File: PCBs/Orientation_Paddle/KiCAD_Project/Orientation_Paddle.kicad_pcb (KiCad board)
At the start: 2 copper layers, 108 x 47 mm, 76 parts, among them J1 NP_Conn_01x04_Relief, J10 1-0000190, J2 1-0001205, J3 NP_Conn_01x03_Relief, J4 NP_Conn_01x02_Relief, J5 NP_Conn_01x02_Relief, J6 NP_Conn_01x04, J7 NP_Conn_01x04, J8 NP_Conn_01x02, J9 1-0000050, U1 1-0001232, U2 1-0001471, U3 1-0000207, U4 1-0000446, U5 1-0000785, Y1 1-0000721

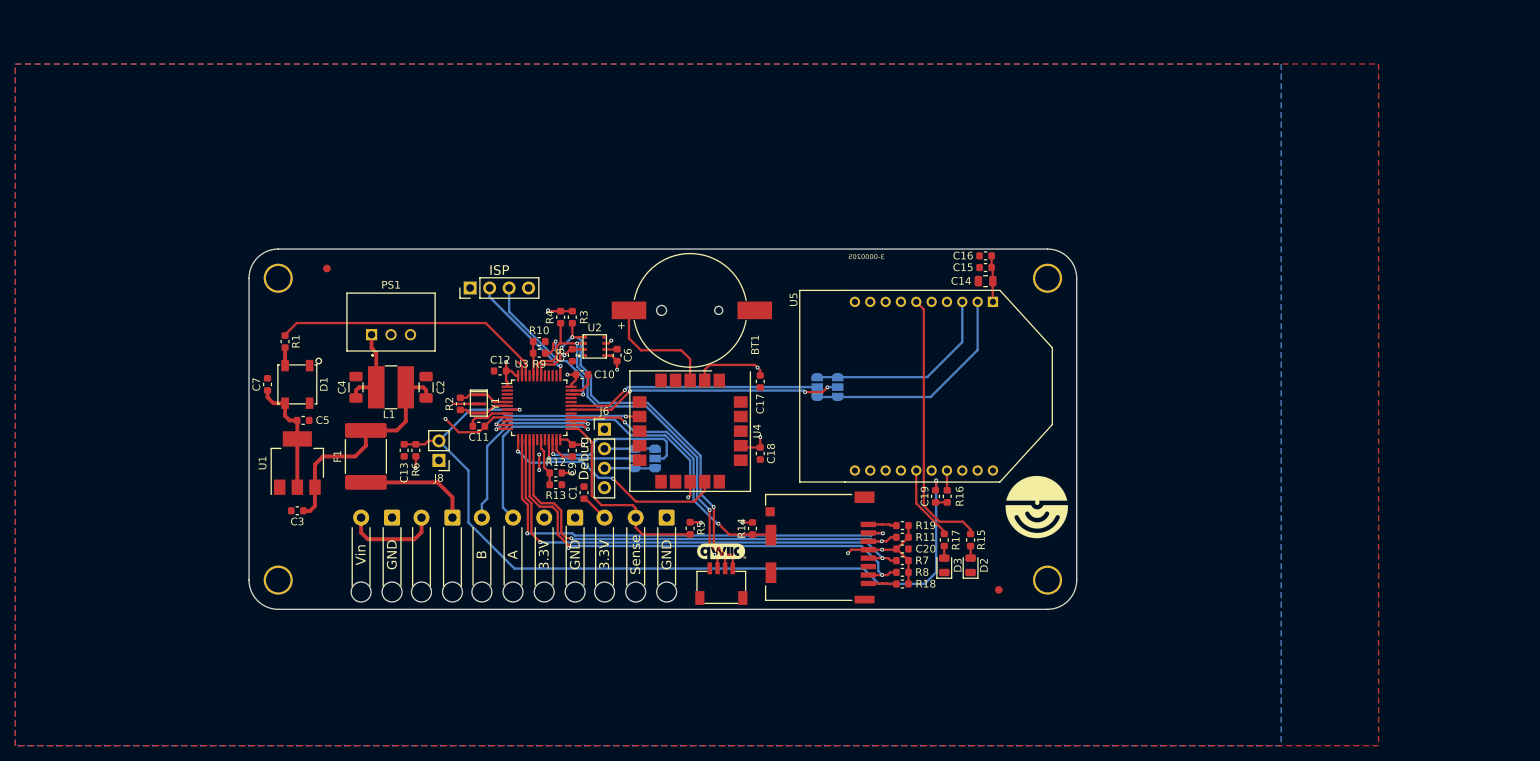
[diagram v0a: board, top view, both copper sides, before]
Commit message: Orientation Paddle Revisions: Board resize to nice numbers Fixed Footprint/Symbols causing ERC Errors Fixed remaining ERC Errors (Schematic and PCB)
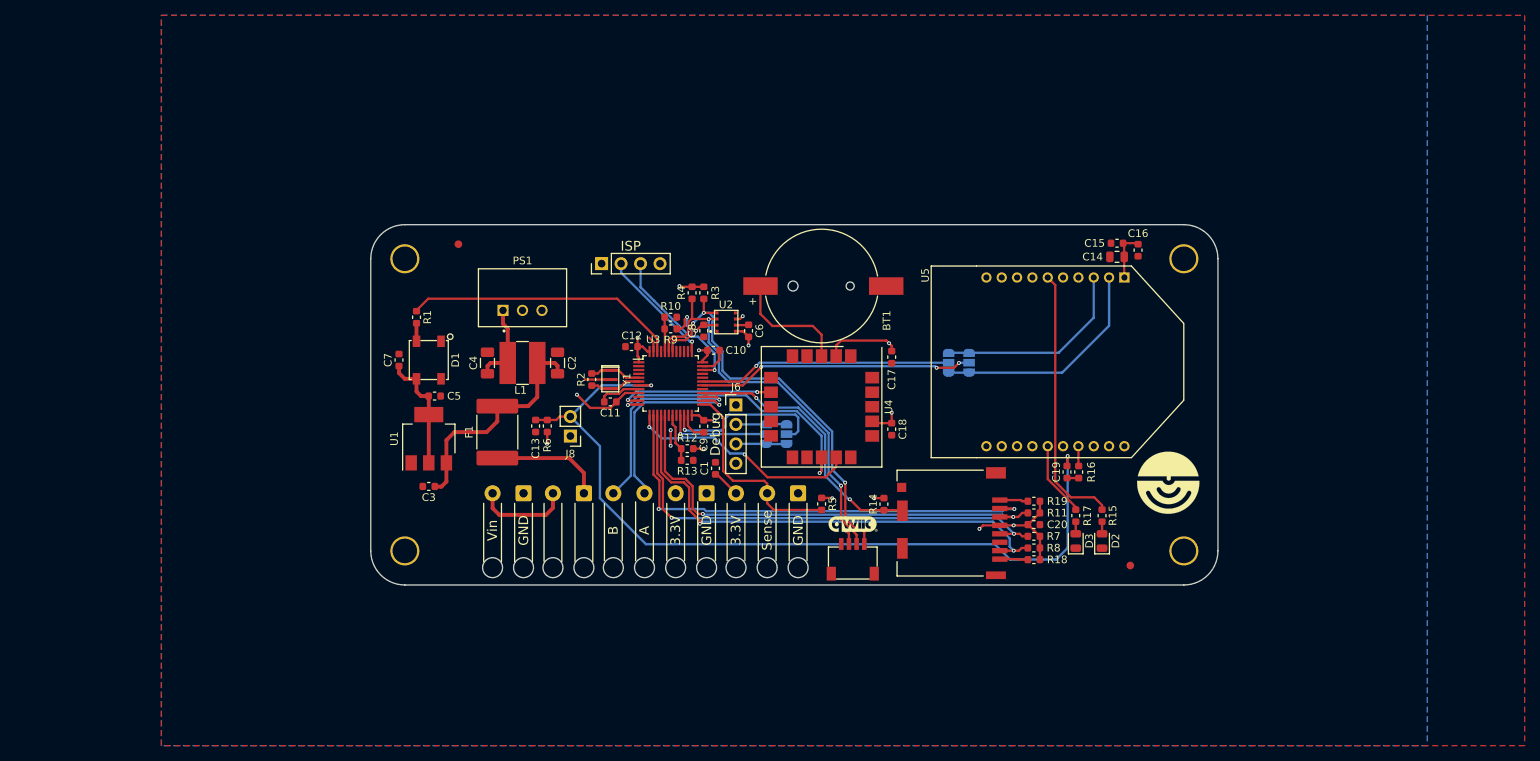
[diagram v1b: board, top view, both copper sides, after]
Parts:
- removed the G*** at (117.5, 139.7)
- added G***: QWIIC, pcb_graphics:5mm qwiic logo, F.Cu at (134.6, 136.1)
- moved C16 19.9 mm to (171.8, 100.5), turned to -90 degrees
- moved H2 18.2 mm to (177.8, 139.7)
- moved H4 18.0 mm to (177.8, 101.6)
- moved FID1 17.4 mm to (170.8, 141.6)
- moved G*** 17.4 mm to (175.8, 130.8)
- moved G*** 17.4 mm to (167.9, 138.6)
- moved J10 17.4 mm to (147.4, 136.3)
- moved J4 17.4 mm to (89.6, 131.6)
- moved J8 17.4 mm to (97.8, 124.7)
- moved R15 17.4 mm to (167.1, 135.1)
- moved R17 17.4 mm to (163.7, 135.1)
- moved R5 17.4 mm to (130.6, 133.6)
- moved BT1 17.4 mm to (130.6, 105.2)
- moved C10 17.4 mm to (116.5, 113.5)
- moved C13 17.4 mm to (93.3, 123.4)
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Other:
- board size 108 x 47 mm -> 110.5 x 47 mm

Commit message: Fixed Orientation Paddle ERC Issues and Copper to Edge Clearence
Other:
- copper layers 2 -> 4
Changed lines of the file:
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@@
 	(generator_version "8.0")
 	(general
-		(thickness 1.6)
+		(thickness 2.446)
 		(legacy_teardrops no)
 	)
@@
 	(layers
 		(0 "F.Cu" signal)
+		(1 "In1.Cu" signal)
+		(2 "In2.Cu" signal)
 		(31 "B.Cu" signal)
 		(32 "B.Adhes" user "B.Adhesive")
@@
 			(layer "dielectric 1"
 				(type "core")
-				(thickness 1.51)
+				(thickness 0.762)
+				(material "FR4")
+				(epsilon_r 4.5)
+				(loss_tangent 0.02)
+			)
+			(layer "In1.Cu"
+				(type "copper")
+				(thickness 0.035)
+			)
+			(layer "dielectric 2"
+				(type "prepreg")
+				(thickness 0.762)
+				(material "FR4")
+				(epsilon_r 4.5)
+				(loss_tangent 0.02)
+			)
+			(layer "In2.Cu"
+				(type "copper")
+				(thickness 0.035)
+			)
+			(layer "dielectric 3"
+				(type "core")
+				(thickness 0.762)
 				(material "FR4")
 				(epsilon_r 4.5)
@@
 			)
 		)
-		(sheetname "Root")
-		(sheetfile "Orientation_Paddle.kicad_sch")
-		(attr exclude_from_pos_files)
+		(attr exclude_from_pos_files exclude_from_bom)
 		(fp_circle
 			(center 0 0)
@@
 			)
 		)
-		(sheetname "Root")
-		(sheetfile "Orientation_Paddle.kicad_sch")
-		(attr exclude_from_pos_files)
+		(attr exclude_from_pos_files exclude_from_bom)
 		(fp_circle
 			(center 0 0)
@@
 			)
 		)
-		(sheetname "Root")
-		(sheetfile "Orientation_Paddle.kicad_sch")
-		(attr exclude_from_pos_files)
+		(attr exclude_from_pos_files exclude_from_bom)
 		(fp_circle
 			(center 0 0)
@@
 			)
 		)
-		(sheetname "Root")
-		(sheetfile "Orientation_Paddle.kicad_sch")
-		(attr exclude_from_pos_files)
+		(attr exclude_from_pos_files exclude_from_bom)
 		(fp_circle
 			(center 0 0)

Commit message: Fixed Orientation Paddle to Have only 2 layer instead of 4
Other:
- copper layers 4 -> 2
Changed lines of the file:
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@@
 	(layers
 		(0 "F.Cu" signal)
-		(1 "In1.Cu" signal)
-		(2 "In2.Cu" signal)
 		(31 "B.Cu" signal)
 		(32 "B.Adhes" user "B.Adhesive")
@@
 			(layer "dielectric 1"
 				(type "core")
-				(thickness 0.762)
-				(material "FR4")
-				(epsilon_r 4.5)
-				(loss_tangent 0.02)
-			)
-			(layer "In1.Cu"
-				(type "copper")
-				(thickness 0.035)
-			)
-			(layer "dielectric 2"
-				(type "prepreg")
-				(thickness 0.762)
-				(material "FR4")
-				(epsilon_r 4.5)
-				(loss_tangent 0.02)
-			)
-			(layer "In2.Cu"
-				(type "copper")
-				(thickness 0.035)
-			)
-			(layer "dielectric 3"
-				(type "core")
-				(thickness 0.762)
+				(thickness 2.356)
 				(material "FR4")
 				(epsilon_r 4.5)
@@
 			(size 3.7973 3.7973)
 			(drill 3.2)
-			(layers "F&B.Cu" "*.Mask")
+			(layers "*.Cu" "*.Mask")
 		)
 	)
@@
 			(size 3.7973 3.7973)
 			(drill 3.2)
-			(layers "F&B.Cu" "*.Mask")
+			(layers "*.Cu" "*.Mask")
 		)
 	)
@@
 			(size 3.7973 3.7973)
 			(drill 3.2)
-			(layers "F&B.Cu" "*.Mask")
+			(layers "*.Cu" "*.Mask")
 		)
 	)
@@
 			(size 3.7973 3.7973)
 			(drill 3.2)
-			(layers "F&B.Cu" "*.Mask")
+			(layers "*.Cu" "*.Mask")
 		)
 	)
